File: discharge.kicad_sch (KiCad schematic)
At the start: 0 parts

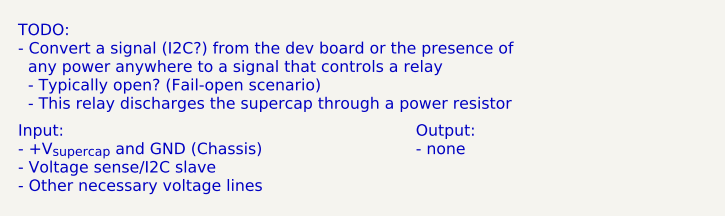
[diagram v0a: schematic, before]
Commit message: Normally open => closed
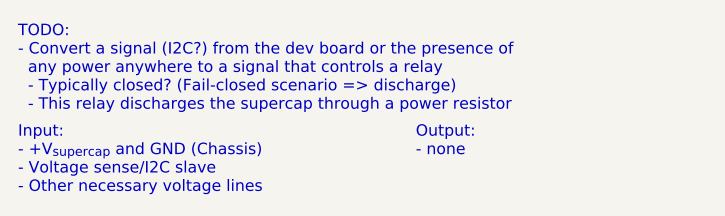
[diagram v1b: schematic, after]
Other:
- note added: "TODO: - Convert a signal (I2C?) from the dev board or the presence of any power anywhere to a signal that controls a relay - Typically closed? (Fail-closed scenario => discharge) - This relay discharges the supercap through a power resistor"
- note removed: "TODO: - Convert a signal (I2C?) from the dev board or the presence of any power anywhere to a signal that controls a relay - Typically open? (Fail-open scenario) - This relay discharges the supercap through a power resistor"
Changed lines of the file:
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@@
 		)
 	)
-	(text "TODO:\n- Convert a signal (I2C?) from the dev board or the presence of\n  any power anywhere to a signal that controls a relay\n  - Typically open? (Fail-open scenario)\n  - This relay discharges the supercap through a power resistor"
+	(text "TODO:\n- Convert a signal (I2C?) from the dev board or the presence of\n  any power anywhere to a signal that controls a relay\n  - Typically closed? (Fail-closed scenario => discharge)\n  - This relay discharges the supercap through a power resistor"
 		(exclude_from_sim no)
 		(at 93.98 90.678 0)

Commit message: started safetydischarge
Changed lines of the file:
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@@
+		)
+	)
+	(hierarchical_label "+V_{supercap}"
+		(shape input)
+		(at 90.17 120.65 180)
+		(fields_autoplaced yes)
+		(effects
+			(font
+				(size 1.27 1.27)
+			)
+			(justify right)
+		)
+	)
+	(symbol
+		(lib_id "power:GNDPWR")
+		(at 90.17 133.35 0)
+		(unit 1)
+		(exclude_from_sim no)
+		(in_bom yes)
+		(on_board yes)
+		(dnp no)
+		(fields_autoplaced yes)
+		(property "Reference" "#PWR099"
+			(at 90.17 138.43 0)
+			(effects
+				(font
+					(size 1.27 1.27)
+				)
+				(hide yes)
+			)
+		)
+		(property "Value" "GNDPWR"
+			(at 90.043 137.16 0)
+			(effects
+				(font
+					(size 1.27 1.27)
+				)
+			)
+		)
+		(property "Footprint" ""
+			(at 90.17 134.62 0)
+			(effects
+				(font
+					(size 1.27 1.27)
+				)
+				(hide yes)
+			)
+		)
+		(property "Datasheet" ""
+			(at 90.17 134.62 0)
+			(effects
+				(font
+					(size 1.27 1.27)
+				)
+				(hide yes)
+			)
+		)
+		(property "Description" "Power symbol creates a global label with name \"GNDPWR\" , global ground"
+			(at 90.17 133.35 0)
+			(effects
+				(font
+					(size 1.27 1.27)
+				)
+				(hide yes)
+			)
+		)
+		(pin "1"
+		)
+		(instances
+			(project "SupercapManager"
+				(path "/6197145b-e7d4-44cc-9d90-537b6501bf60/ed9bb12b-3108-48de-97f5-99577caac45c"
+					(reference "#PWR099")
+					(unit 1)
+				)
+			)
 		)
 	)

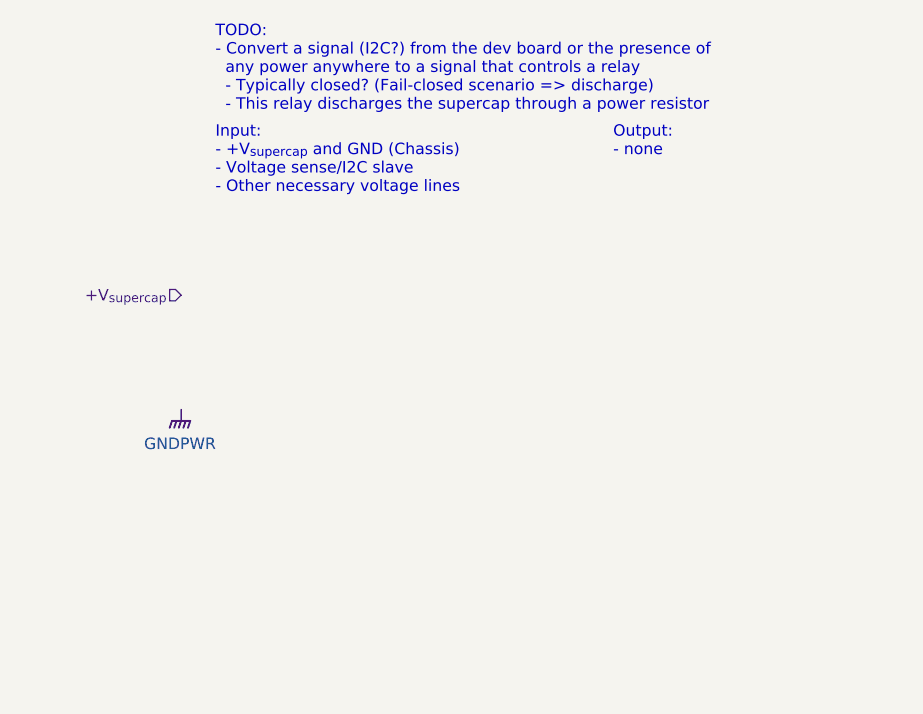
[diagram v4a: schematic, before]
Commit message: updated discharge subsheet
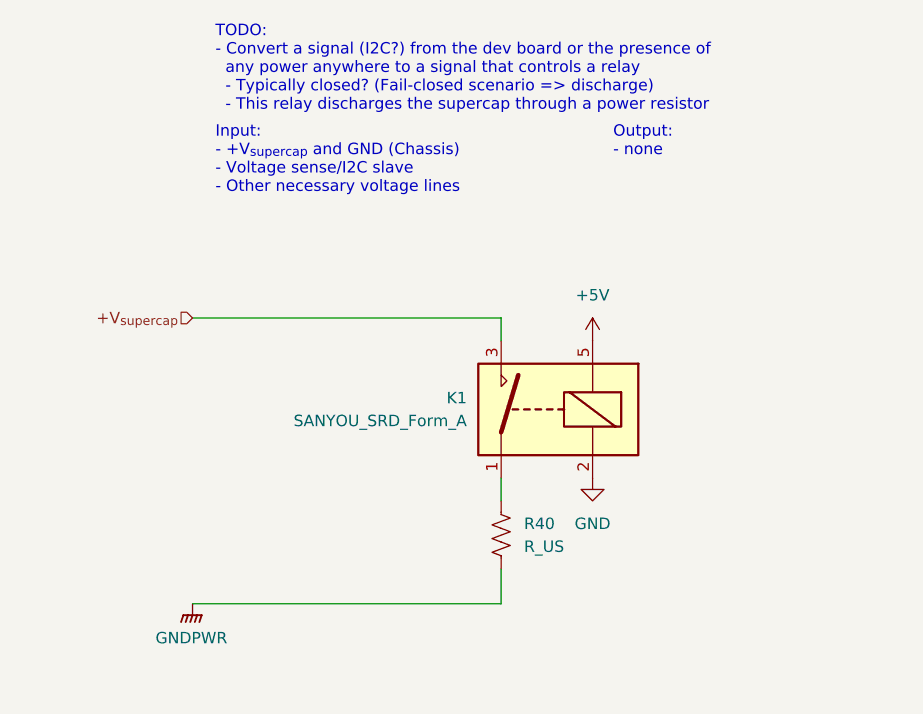
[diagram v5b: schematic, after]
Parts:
- added K1: SANYOU_SRD_Form_A, Relay_THT:Relay_SPST_SANYOU_SRD_Series_Form_A, symbol Relay:SANYOU_SRD_Form_A
- added R40: R_US, symbol Device:R_US
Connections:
- net +V_{supercap}: now also K1.3
- net GNDPWR: now also R40.2
- new net: K1.1, R40.1
- new net +5V: K1.5
- new net GND: K1.2

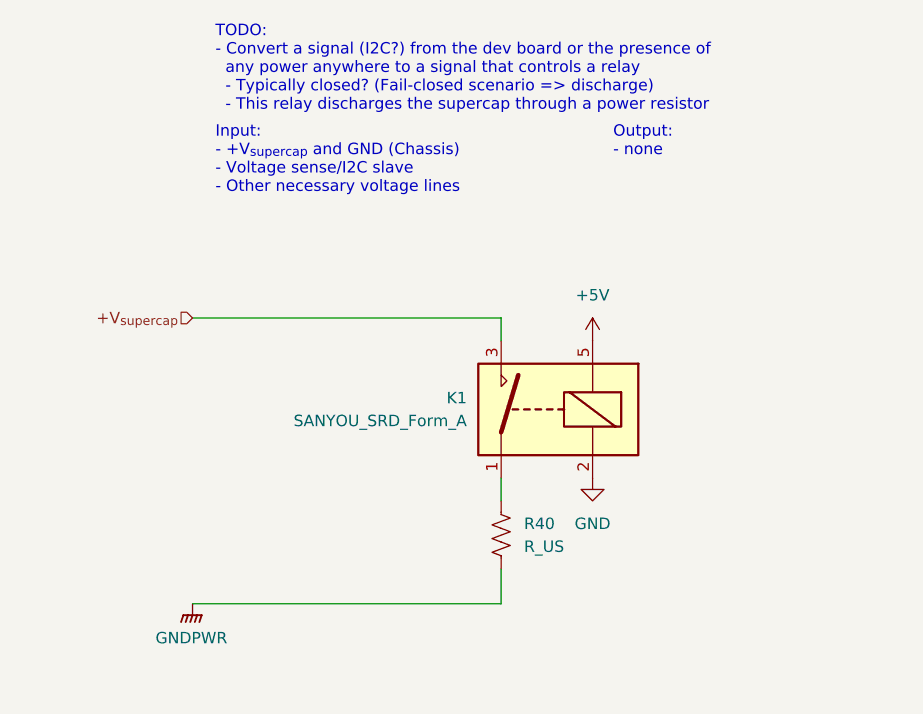
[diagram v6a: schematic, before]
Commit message: Updating discharge circuit to work with +24V power
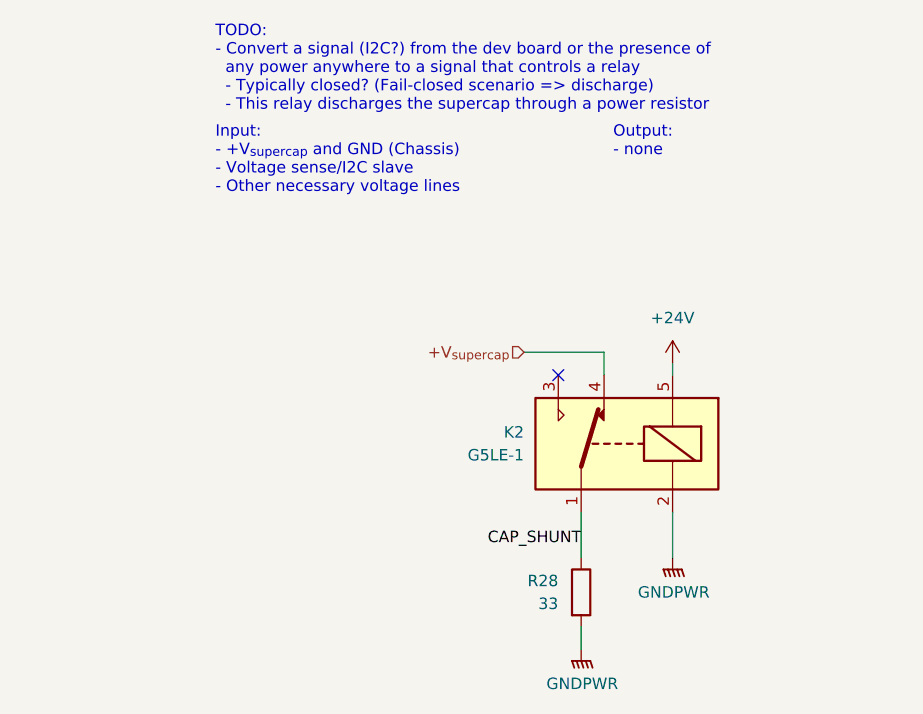
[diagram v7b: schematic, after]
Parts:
- removed K1: SANYOU_SRD_Form_A, Relay_THT:Relay_SPST_SANYOU_SRD_Series_Form_A, symbol Relay:SANYOU_SRD_Form_A
- removed R40: R_US, symbol Device:R_US
- added K2: G5LE-1, Relay_THT:Relay_SPDT_SANYOU_SRD_Series_Form_C, symbol Relay:G5LE-1
- added R28: 33, Resistor_SMD:R_1210_3225Metric_Pad1.30x2.65mm_HandSolder, symbol Device:R
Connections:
- net +V_{supercap}: now also K2.4
- net GNDPWR: now also K2.2, R28.2
- new net +24V: K2.5
- new net CAP_SHUNT: K2.1, R28.1
- no-connect marks 0 -> 1

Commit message: Renumber components
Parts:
- renumbered K2 to K1, R28 to R22
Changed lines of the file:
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@@
 		(dnp no)
 		(fields_autoplaced yes)
-		(property "Reference" "#PWR065"
+		(property "Reference" "#PWR042"
 			(at 134.62 165.1 0)
 			(effects
@@
 			(project "SupercapManager"
 				(path "/6197145b-e7d4-44cc-9d90-537b6501bf60/ed9bb12b-3108-48de-97f5-99577caac45c"
-					(reference "#PWR065")
+					(reference "#PWR042")
 					(unit 1)
 				)
@@
 		(dnp no)
 		(fields_autoplaced yes)
-		(property "Reference" "#PWR058"
+		(property "Reference" "#PWR040"
 			(at 144.78 132.08 0)
 			(effects
@@
 			(project ""
 				(path "/6197145b-e7d4-44cc-9d90-537b6501bf60/ed9bb12b-3108-48de-97f5-99577caac45c"
-					(reference "#PWR058")
+					(reference "#PWR040")
 					(unit 1)
 				)
@@
 		(dnp no)
 		(fields_autoplaced yes)
-		(property "Reference" "K2"
+		(property "Reference" "K1"
 			(at 128.27 135.8899 0)
 			(effects
@@
 			(project "SupercapManager"
 				(path "/6197145b-e7d4-44cc-9d90-537b6501bf60/ed9bb12b-3108-48de-97f5-99577caac45c"
-					(reference "K2")
+					(reference "K1")
 					(unit 1)
 				)
@@
 		(on_board yes)
 		(dnp no)
-		(property "Reference" "R28"
+		(property "Reference" "R22"
 			(at 132.08 152.3999 0)
 			(effects
@@
 			(project ""
 				(path "/6197145b-e7d4-44cc-9d90-537b6501bf60/ed9bb12b-3108-48de-97f5-99577caac45c"
-					(reference "R28")
+					(reference "R22")
 					(unit 1)
 				)
@@
 		(dnp no)
 		(fields_autoplaced yes)
-		(property "Reference" "#PWR064"
+		(property "Reference" "#PWR041"
 			(at 144.78 154.94 0)
 			(effects
@@
 			(project "SupercapManager"
 				(path "/6197145b-e7d4-44cc-9d90-537b6501bf60/ed9bb12b-3108-48de-97f5-99577caac45c"
-					(reference "#PWR064")
-					(unit 1)
-				)
+					(reference "#PWR041")
+					(unit 1)
+				)
